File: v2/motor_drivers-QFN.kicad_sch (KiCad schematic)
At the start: 24 parts, among them IC6 DA7281-00FVC, M1 M1, M1 M2, M1 M3, M1 M4

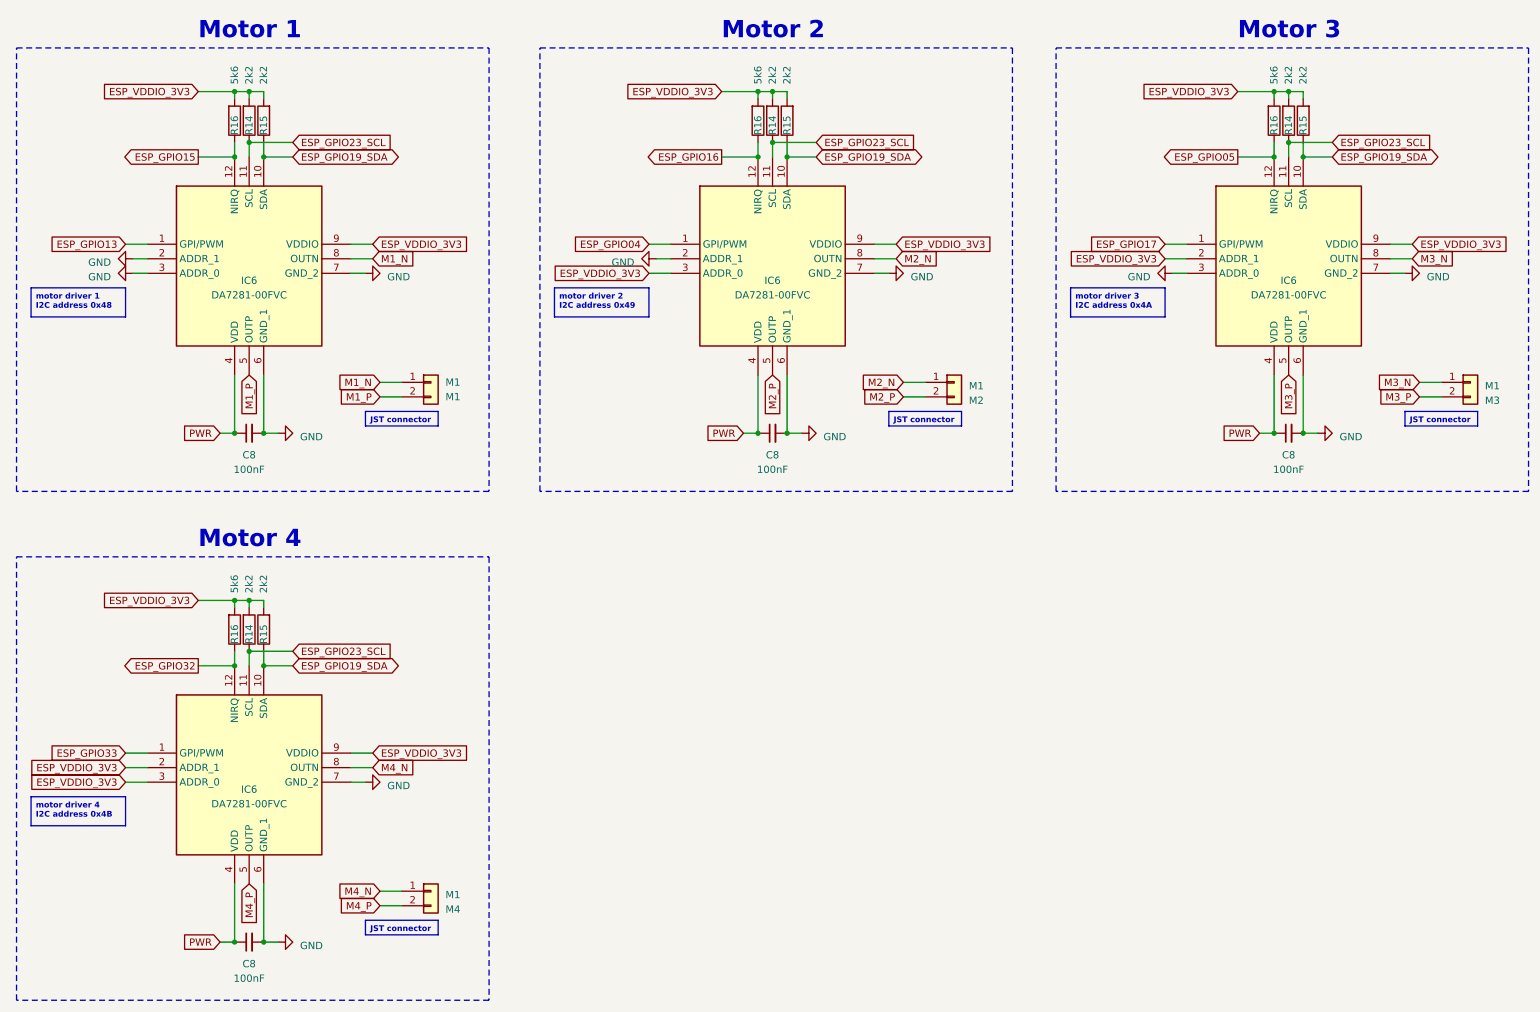
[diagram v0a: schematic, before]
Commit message: start PCB layout
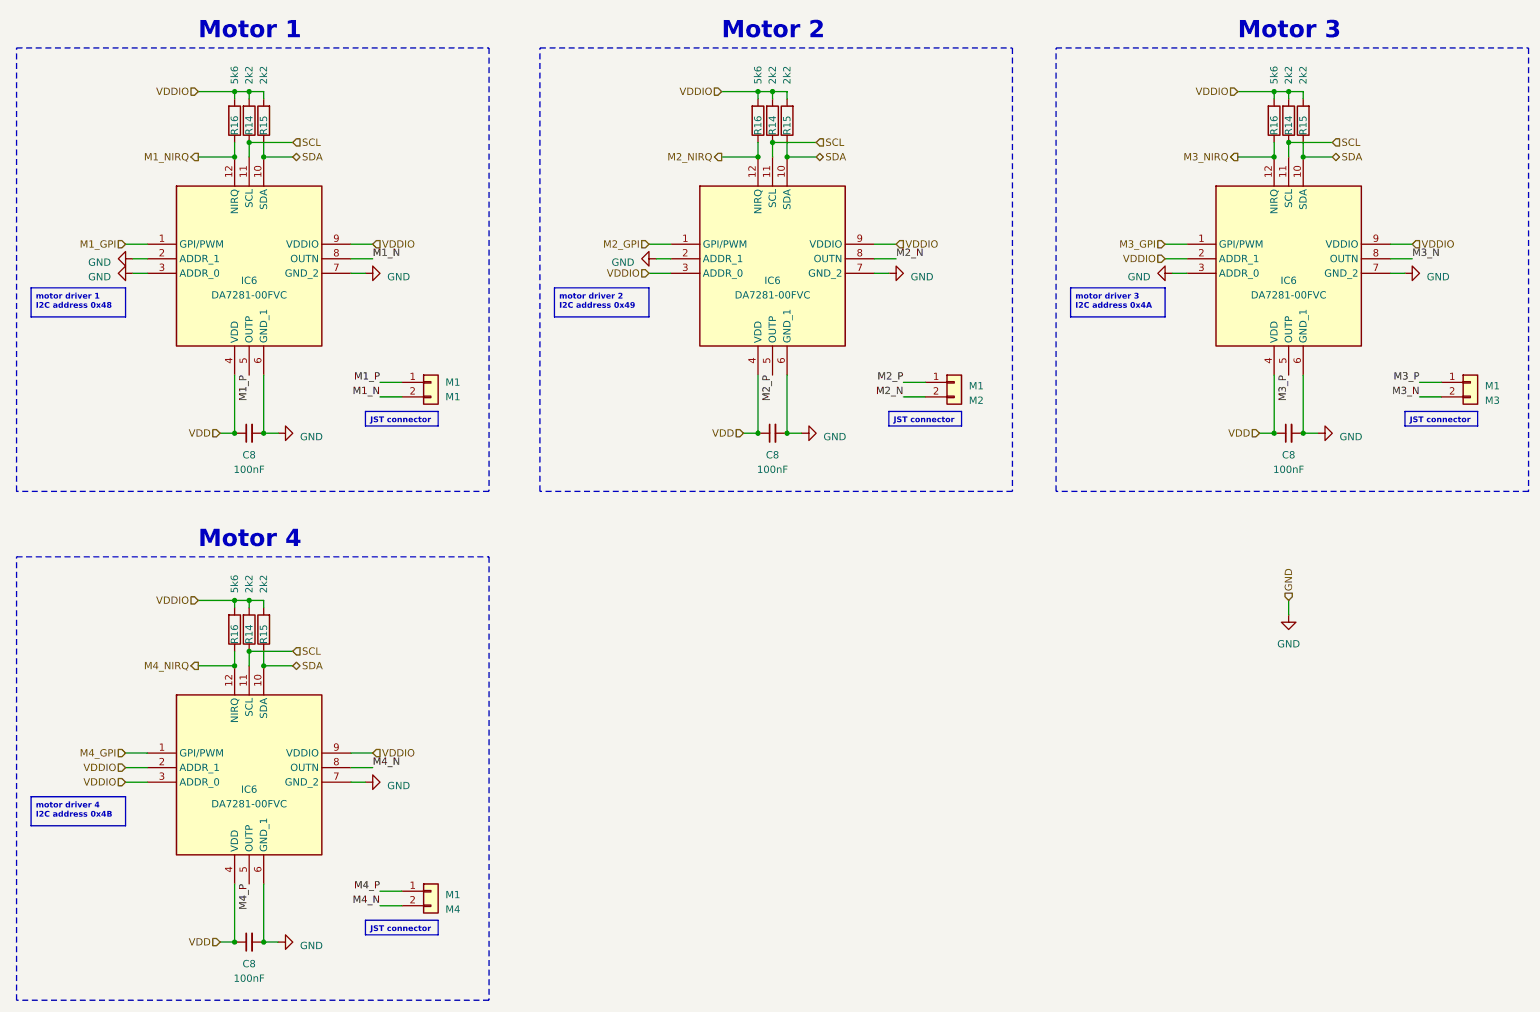
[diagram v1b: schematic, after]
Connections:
- net M1_N: now also M1.2 (Pin_2); no longer M1.1 (Pin_1)
- net M1_P: now also M1.1 (Pin_1); no longer M1.2 (Pin_2)
- net M2_N: now also M1.2 (Pin_2); no longer M1.1 (Pin_1)
- net M2_P: now also M1.1 (Pin_1); no longer M1.2 (Pin_2)
- net M3_N: now also M1.2 (Pin_2); no longer M1.1 (Pin_1)
- net M3_P: now also M1.1 (Pin_1); no longer M1.2 (Pin_2)
- net M4_N: now also M1.2 (Pin_2); no longer M1.1 (Pin_1)
- net M4_P: now also M1.1 (Pin_1); no longer M1.2 (Pin_2)
- net ESP_GPIO04 renamed M2_GPI
- net ESP_GPIO05 renamed M3_NIRQ
- net ESP_GPIO13 renamed M1_GPI
- net ESP_GPIO15 renamed M1_NIRQ
- net ESP_GPIO16 renamed M2_NIRQ
- net ESP_GPIO17 renamed M3_GPI
- net ESP_GPIO19_SDA renamed SDA
- net ESP_GPIO23_SCL renamed SCL
- net ESP_GPIO32 renamed M4_NIRQ
- net ESP_GPIO33 renamed M4_GPI
- net ESP_VDDIO_3V3 renamed VDDIO
- net PWR renamed VDD
